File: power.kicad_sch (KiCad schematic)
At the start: 11 parts, among them J1 Conn_01x02_Pin, T1 Transformer_1P_1S

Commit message: Done upto shunt circuit, H-bridge, remaining Loogic
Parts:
- added C10: 0.33uF, symbol Device:C_Polarized
- added C11: 0.1uF, symbol Device:C_Polarized_Small
- added C12, C13: 10uF, symbol Device:C_Polarized_Small_US
- added C14: C, symbol Device:C
- added C9: 220uF, symbol Device:C_Small
- added D10: D_Schottky, symbol Device:D_Schottky
- added L1: 33uH, symbol Device:L
- added R10: 8.75K, symbol Device:R
- added R9: 1K, symbol Device:R
- added U6: LM2596S-ADJ, Package_TO_SOT_SMD:TO-263-5_TabPin3, symbol Regulator_Switching:LM2596S-ADJ
- added U7: LM7805_TO220, Package_TO_SOT_THT:TO-220-3_Vertical, symbol Regulator_Linear:LM7805_TO220
- added U8: LM1117DT-3.3, Package_TO_SOT_SMD:TO-252-3_TabPin2, symbol Regulator_Linear:LM1117DT-3.3
- C3: value C -> 0.22uF, 275V
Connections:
- net at C3.2, C5.1, FL1.3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: now also D1.2
- net 24V: now reaches C1.1, C2.1, D1.1 (+)
- net 24V: now also U6.1 (VIN)
- net GND: now reaches C1.2, C2.2, D1.3 (-)
- net GND: now also C10.2, C11.2, C12.2, C13.2, C9.2, D10.2 (A), R9.1, U6.3 (GND), U6.5 (~{ON}/OFF), U7.2 (GND), U8.1 (GND)
- net at C4.2, C5.2, J1.3 (Pin_3): no longer D1.2
- new net: D10.1 (K), L1.1, U6.2 (OUT)
- new net: R10.1, R9.2, U6.4 (FB)
- new net 12V: C10.1, C12.1, C9.1, L1.2, R10.2, U7.1 (VI), U8.3 (VI)
- new net 3V3: C13.1, U8.2 (VO)
- new net 5V: C11.1, U7.3 (VO)
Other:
- note added: "12V OUTPUT BUCK CONVERTER"
- note added: "3V3 Regulator"
- note added: "5V Regulator"
- moved on the sheet: C1, C2, C3, C4, C5, D1, F1, FL1, J1, RV1, T1

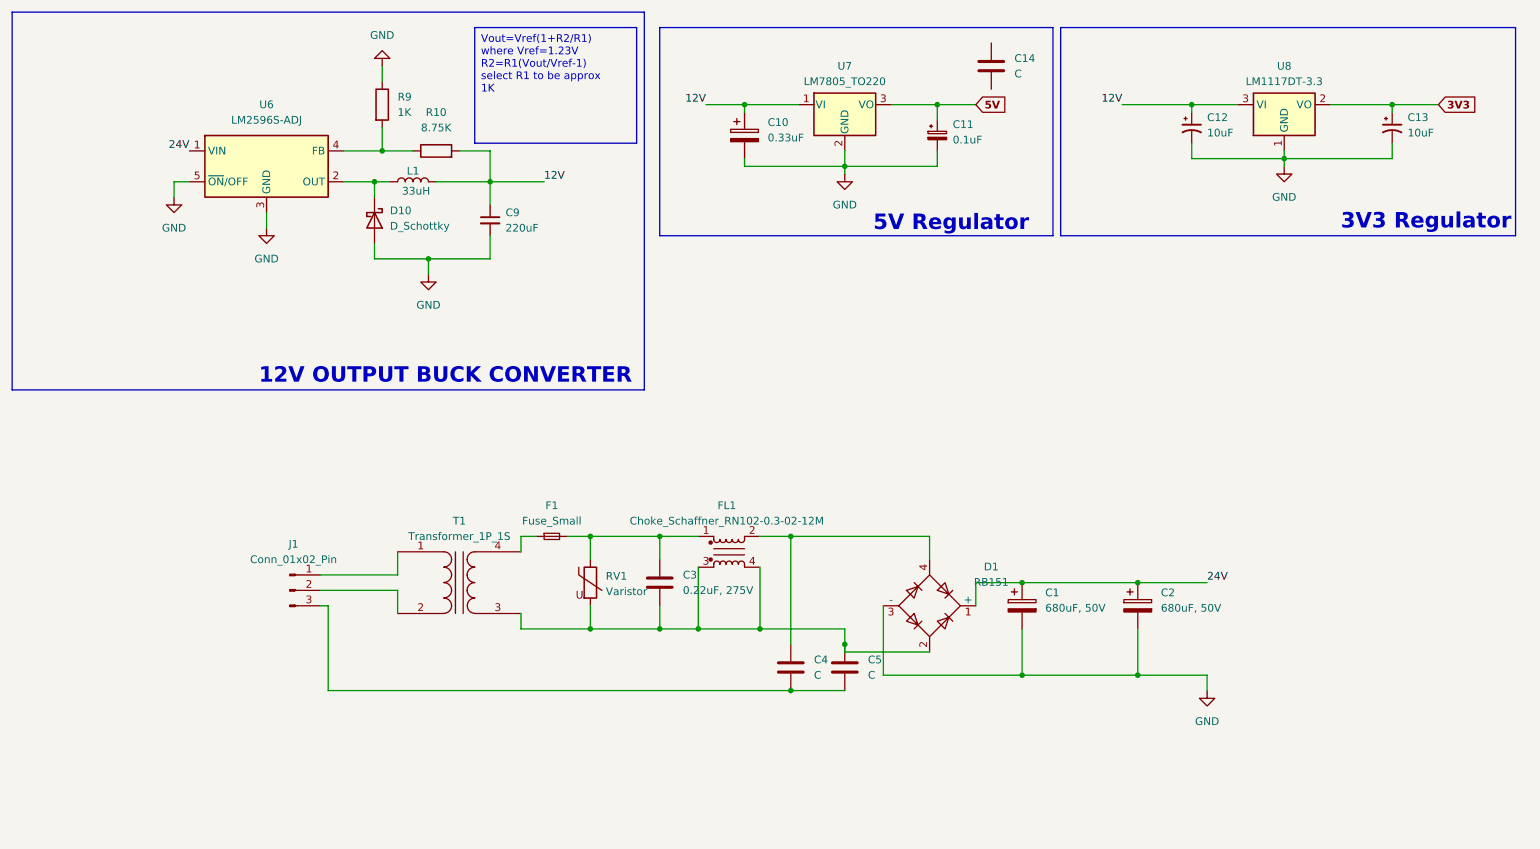
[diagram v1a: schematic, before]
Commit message: Finished all parts of schematic: power, H-bridge, logic and shunt schematics
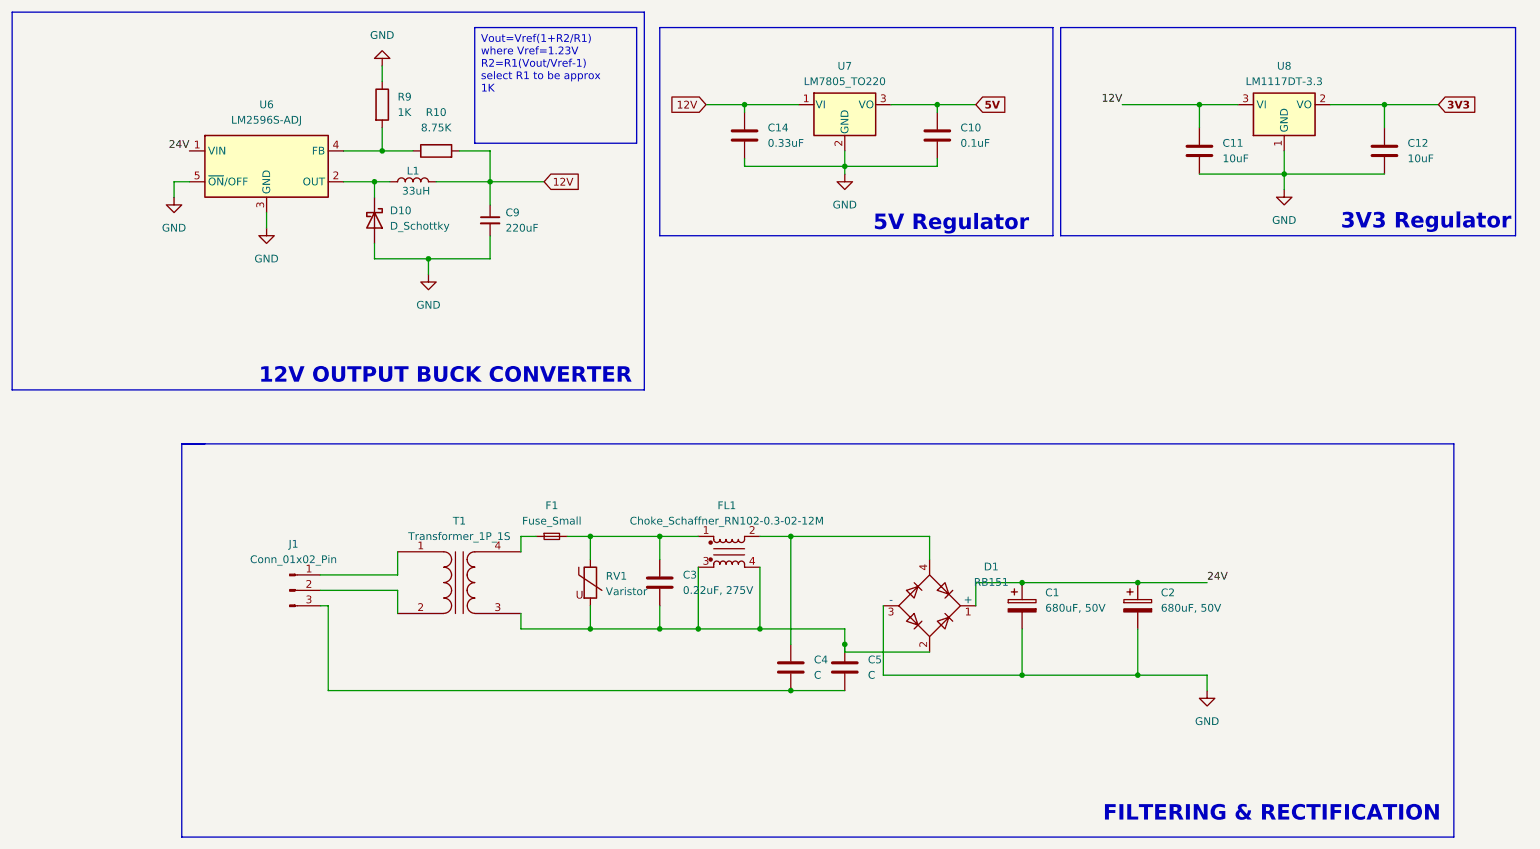
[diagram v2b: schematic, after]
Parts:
- removed C10: 0.33uF, symbol Device:C_Polarized
- removed C11: 0.1uF, symbol Device:C_Polarized_Small
- removed C12, C13: 10uF, symbol Device:C_Polarized_Small_US
- added C10: 0.1uF, symbol Device:C
- added C11, C12: 10uF, symbol Device:C
- C14: value C -> 0.33uF
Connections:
- net 12V: now also C14.1, C11.1
- net 3V3: now also C12.1
- net 5V: now also C10.1
- net GND: now also C14.2, C10.2, C11.2, C12.2
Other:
- note added: "FILTERING & RECTIFICATION"
- moved on the sheet: C14
